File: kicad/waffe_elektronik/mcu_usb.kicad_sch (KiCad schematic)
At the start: 11 parts, among them J3 USB-C (Flashen + Laden), SW3 RESET, SW4 BOOT, U12 USBLC6-2SC6, U4 ESP32-S3-WROOM-1-N16R8

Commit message: Platine: günstigere JLC-Teile, Option ESP32-S3-WROOM-1U mit externer Antenne
- Flash ZD35Q1GC-IB, Kondensatoren/Dioden/Widerstände auf Basic-Teile und 0402, Layout angepasst
- WROOM-1U auf demselben Footprint: eigene JLCPCB-BOM/CPL (Modulmitte 3,15 mm versetzt),
  Mouser-Option mit Pigtail RP-SMA/U.FL und Knick-Stabantenne, 3D-Modell des 1U
- Gerber, BOM, CPL, Renders und Bestelllisten neu erzeugt

Co-Authored-By: Claude Opus 5.5 <noreply@anthropic.com>
Claude-Session: https://claude.ai/code/session_01KkZzubjLKyW9odUwvmxTog
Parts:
- SW3, SW4: LCSC C231329 -> (none)
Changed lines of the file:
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@@
     (instances
       (project "waffe_elektronik"
-        (path "/117486d7-9cbb-4cb5-8faf-1b6e58d9c176"
+        (path "/1905d055-ea1f-4733-9037-b305b5c29de9"
           (reference "U4") (unit 1)
         )
@@
     (instances
       (project "waffe_elektronik"
-        (path "/117486d7-9cbb-4cb5-8faf-1b6e58d9c176"
+        (path "/1905d055-ea1f-4733-9037-b305b5c29de9"
           (reference "#PWR27") (unit 1)
         )
@@
     (instances
       (project "waffe_elektronik"
-        (path "/117486d7-9cbb-4cb5-8faf-1b6e58d9c176"
+        (path "/1905d055-ea1f-4733-9037-b305b5c29de9"
           (reference "C17") (unit 1)
         )
@@
     (instances
       (project "waffe_elektronik"
-        (path "/117486d7-9cbb-4cb5-8faf-1b6e58d9c176"
+        (path "/1905d055-ea1f-4733-9037-b305b5c29de9"
           (reference "#PWR28") (unit 1)
         )
@@
     (instances
       (project "waffe_elektronik"
-        (path "/117486d7-9cbb-4cb5-8faf-1b6e58d9c176"
+        (path "/1905d055-ea1f-4733-9037-b305b5c29de9"
           (reference "C18") (unit 1)
         )
@@
     (instances
       (project "waffe_elektronik"
-        (path "/117486d7-9cbb-4cb5-8faf-1b6e58d9c176"
+        (path "/1905d055-ea1f-4733-9037-b305b5c29de9"
           (reference "#PWR29") (unit 1)
         )
@@
     (instances
       (project "waffe_elektronik"
-        (path "/117486d7-9cbb-4cb5-8faf-1b6e58d9c176"
+        (path "/1905d055-ea1f-4733-9037-b305b5c29de9"
           (reference "#PWR30") (unit 1)
         )
@@
     (instances
       (project "waffe_elektronik"
-        (path "/117486d7-9cbb-4cb5-8faf-1b6e58d9c176"
+        (path "/1905d055-ea1f-4733-9037-b305b5c29de9"
           (reference "R21") (unit 1)
         )
@@
     (instances
       (project "waffe_elektronik"
-        (path "/117486d7-9cbb-4cb5-8faf-1b6e58d9c176"
+        (path "/1905d055-ea1f-4733-9037-b305b5c29de9"
           (reference "#PWR31") (unit 1)
         )
@@
     (instances
       (project "waffe_elektronik"
-        (path "/117486d7-9cbb-4cb5-8faf-1b6e58d9c176"
+        (path "/1905d055-ea1f-4733-9037-b305b5c29de9"
           (reference "C16") (unit 1)
         )
@@
     (instances
       (project "waffe_elektronik"
-        (path "/117486d7-9cbb-4cb5-8faf-1b6e58d9c176"
+        (path "/1905d055-ea1f-4733-9037-b305b5c29de9"
           (reference "#PWR32") (unit 1)
         )
@@
       (effects (font (size 1.27 1.27)) hide)
     )
-    (property "LCSC" "C231329" (at 0 0 0)
-      (effects (font (size 1.27 1.27)) hide)
-    )
-    (pin "1")
-    (pin "2")
-    (instances
-      (project "waffe_elektronik"
-        (path "/117486d7-9cbb-4cb5-8faf-1b6e58d9c176"
+    (pin "1")
+    (pin "2")
+    (instances
+      (project "waffe_elektronik"
+        (path "/1905d055-ea1f-4733-9037-b305b5c29de9"
           (reference "SW3") (unit 1)
         )
@@
     (instances
       (project "waffe_elektronik"
-        (path "/117486d7-9cbb-4cb5-8faf-1b6e58d9c176"
+        (path "/1905d055-ea1f-4733-9037-b305b5c29de9"
           (reference "#PWR33") (unit 1)
         )
@@
       (effects (font (size 1.27 1.27)) hide)
     )
-    (property "LCSC" "C231329" (at 0 0 0)
-      (effects (font (size 1.27 1.27)) hide)
-    )
-    (pin "1")
-    (pin "2")
-    (instances
-      (project "waffe_elektronik"
-        (path "/117486d7-9cbb-4cb5-8faf-1b6e58d9c176"
+    (pin "1")
+    (pin "2")
+    (instances
+      (project "waffe_elektronik"
+        (path "/1905d055-ea1f-4733-9037-b305b5c29de9"
           (reference "SW4") (unit 1)
         )
@@
     (instances
       (project "waffe_elektronik"
-        (path "/117486d7-9cbb-4cb5-8faf-1b6e58d9c176"
+        (path "/1905d055-ea1f-4733-9037-b305b5c29de9"
           (reference "#PWR34") (unit 1)
         )
@@
     (instances
       (project "waffe_elektronik"
-        (path "/117486d7-9cbb-4cb5-8faf-1b6e58d9c176"
+        (path "/1905d055-ea1f-4733-9037-b305b5c29de9"
           (reference "J3") (unit 1)
         )
@@
     (instances
       (project "waffe_elektronik"
-        (path "/117486d7-9cbb-4cb5-8faf-1b6e58d9c176"
+        (path "/1905d055-ea1f-4733-9037-b305b5c29de9"
           (reference "#PWR35") (unit 1)
         )
@@
     (instances
       (project "waffe_elektronik"
-        (path "/117486d7-9cbb-4cb5-8faf-1b6e58d9c176"
+        (path "/1905d055-ea1f-4733-9037-b305b5c29de9"
           (reference "R23") (unit 1)
         )
@@
     (instances
       (project "waffe_elektronik"
-        (path "/117486d7-9cbb-4cb5-8faf-1b6e58d9c176"
+        (path "/1905d055-ea1f-4733-9037-b305b5c29de9"
           (reference "#PWR36") (unit 1)
         )
@@
     (instances
       (project "waffe_elektronik"
-        (path "/117486d7-9cbb-4cb5-8faf-1b6e58d9c176"
+        (path "/1905d055-ea1f-4733-9037-b305b5c29de9"
           (reference "R22") (unit 1)
         )
@@
     (instances
       (project "waffe_elektronik"
-        (path "/117486d7-9cbb-4cb5-8faf-1b6e58d9c176"
+        (path "/1905d055-ea1f-4733-9037-b305b5c29de9"
           (reference "#PWR37") (unit 1)
         )
@@
     (instances
       (project "waffe_elektronik"
-        (path "/117486d7-9cbb-4cb5-8faf-1b6e58d9c176"
+        (path "/1905d055-ea1f-4733-9037-b305b5c29de9"
           (reference "U12") (unit 1)
         )
@@
     (instances
       (project "waffe_elektronik"
-        (path "/117486d7-9cbb-4cb5-8faf-1b6e58d9c176"
+        (path "/1905d055-ea1f-4733-9037-b305b5c29de9"
           (reference "#PWR38") (unit 1)
         )
@@
     (instances
       (project "waffe_elektronik"
-        (path "/117486d7-9cbb-4cb5-8faf-1b6e58d9c176"
+        (path "/1905d055-ea1f-4733-9037-b305b5c29de9"
           (reference "#PWR39") (unit 1)
         )
@@
     (instances
       (project "waffe_elektronik"
-        (path "/117486d7-9cbb-4cb5-8faf-1b6e58d9c176"
+        (path "/1905d055-ea1f-4733-9037-b305b5c29de9"
           (reference "#PWR40") (unit 1)
         )

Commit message: Fertigung: JLCPCB-BOM/CPL mit allen Steckern und Tastern (Variante komplett)
- Handlötteile tragen im Schaltplan das Feld "LCSC Hand" statt "LCSC", build_board.py übernimmt es
- jlc_fab.py schreibt zusätzlich *_komplett und *_komplett_externe_antenne (79 Teile, 20 Extended),
  --check prüft den Bedarf der Komplett-Variante; Rotationskorrektur 180° für JST-SH (ungeprüft)
- Schaltplan und Platine neu erzeugt (Geometrie unverändert), Gerber neu, Doku angepasst

Co-Authored-By: Claude Opus 5.5 <noreply@anthropic.com>
Claude-Session: https://claude.ai/code/session_01KkZzubjLKyW9odUwvmxTog
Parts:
- SW3, SW4: LCSC Hand (none) -> C231329
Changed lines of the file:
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@@
     (instances
       (project "waffe_elektronik"
-        (path "/1905d055-ea1f-4733-9037-b305b5c29de9"
+        (path "/3bcff933-1787-416b-898f-1e2cea15666c"
           (reference "U4") (unit 1)
         )
@@
     (instances
       (project "waffe_elektronik"
-        (path "/1905d055-ea1f-4733-9037-b305b5c29de9"
+        (path "/3bcff933-1787-416b-898f-1e2cea15666c"
           (reference "#PWR27") (unit 1)
         )
@@
     (instances
       (project "waffe_elektronik"
-        (path "/1905d055-ea1f-4733-9037-b305b5c29de9"
+        (path "/3bcff933-1787-416b-898f-1e2cea15666c"
           (reference "C17") (unit 1)
         )
@@
     (instances
       (project "waffe_elektronik"
-        (path "/1905d055-ea1f-4733-9037-b305b5c29de9"
+        (path "/3bcff933-1787-416b-898f-1e2cea15666c"
           (reference "#PWR28") (unit 1)
         )
@@
     (instances
       (project "waffe_elektronik"
-        (path "/1905d055-ea1f-4733-9037-b305b5c29de9"
+        (path "/3bcff933-1787-416b-898f-1e2cea15666c"
           (reference "C18") (unit 1)
         )
@@
     (instances
       (project "waffe_elektronik"
-        (path "/1905d055-ea1f-4733-9037-b305b5c29de9"
+        (path "/3bcff933-1787-416b-898f-1e2cea15666c"
           (reference "#PWR29") (unit 1)
         )
@@
     (instances
       (project "waffe_elektronik"
-        (path "/1905d055-ea1f-4733-9037-b305b5c29de9"
+        (path "/3bcff933-1787-416b-898f-1e2cea15666c"
           (reference "#PWR30") (unit 1)
         )
@@
     (instances
       (project "waffe_elektronik"
-        (path "/1905d055-ea1f-4733-9037-b305b5c29de9"
+        (path "/3bcff933-1787-416b-898f-1e2cea15666c"
           (reference "R21") (unit 1)
         )
@@
     (instances
       (project "waffe_elektronik"
-        (path "/1905d055-ea1f-4733-9037-b305b5c29de9"
+        (path "/3bcff933-1787-416b-898f-1e2cea15666c"
           (reference "#PWR31") (unit 1)
         )
@@
     (instances
       (project "waffe_elektronik"
-        (path "/1905d055-ea1f-4733-9037-b305b5c29de9"
+        (path "/3bcff933-1787-416b-898f-1e2cea15666c"
           (reference "C16") (unit 1)
         )
@@
     (instances
       (project "waffe_elektronik"
-        (path "/1905d055-ea1f-4733-9037-b305b5c29de9"
+        (path "/3bcff933-1787-416b-898f-1e2cea15666c"
           (reference "#PWR32") (unit 1)
         )
@@
       (effects (font (size 1.27 1.27)) hide)
     )
-    (pin "1")
-    (pin "2")
-    (instances
-      (project "waffe_elektronik"
-        (path "/1905d055-ea1f-4733-9037-b305b5c29de9"
+    (property "LCSC Hand" "C231329" (at 0 0 0)
+      (effects (font (size 1.27 1.27)) hide)
+    )
+    (pin "1")
+    (pin "2")
+    (instances
+      (project "waffe_elektronik"
+        (path "/3bcff933-1787-416b-898f-1e2cea15666c"
           (reference "SW3") (unit 1)
         )
@@
     (instances
       (project "waffe_elektronik"
-        (path "/1905d055-ea1f-4733-9037-b305b5c29de9"
+        (path "/3bcff933-1787-416b-898f-1e2cea15666c"
           (reference "#PWR33") (unit 1)
         )
@@
       (effects (font (size 1.27 1.27)) hide)
     )
-    (pin "1")
-    (pin "2")
-    (instances
-      (project "waffe_elektronik"
-        (path "/1905d055-ea1f-4733-9037-b305b5c29de9"
+    (property "LCSC Hand" "C231329" (at 0 0 0)
+      (effects (font (size 1.27 1.27)) hide)
+    )
+    (pin "1")
+    (pin "2")
+    (instances
+      (project "waffe_elektronik"
+        (path "/3bcff933-1787-416b-898f-1e2cea15666c"
           (reference "SW4") (unit 1)
         )
@@
     (instances
       (project "waffe_elektronik"
-        (path "/1905d055-ea1f-4733-9037-b305b5c29de9"
+        (path "/3bcff933-1787-416b-898f-1e2cea15666c"
           (reference "#PWR34") (unit 1)
         )
@@
     (instances
       (project "waffe_elektronik"
-        (path "/1905d055-ea1f-4733-9037-b305b5c29de9"
+        (path "/3bcff933-1787-416b-898f-1e2cea15666c"
           (reference "J3") (unit 1)
         )
@@
     (instances
       (project "waffe_elektronik"
-        (path "/1905d055-ea1f-4733-9037-b305b5c29de9"
+        (path "/3bcff933-1787-416b-898f-1e2cea15666c"
           (reference "#PWR35") (unit 1)
         )
@@
     (instances
       (project "waffe_elektronik"
-        (path "/1905d055-ea1f-4733-9037-b305b5c29de9"
+        (path "/3bcff933-1787-416b-898f-1e2cea15666c"
           (reference "R23") (unit 1)
         )
@@
     (instances
       (project "waffe_elektronik"
-        (path "/1905d055-ea1f-4733-9037-b305b5c29de9"
+        (path "/3bcff933-1787-416b-898f-1e2cea15666c"
           (reference "#PWR36") (unit 1)
         )
@@
     (instances
       (project "waffe_elektronik"
-        (path "/1905d055-ea1f-4733-9037-b305b5c29de9"
+        (path "/3bcff933-1787-416b-898f-1e2cea15666c"
           (reference "R22") (unit 1)
         )
@@
     (instances
       (project "waffe_elektronik"
-        (path "/1905d055-ea1f-4733-9037-b305b5c29de9"
+        (path "/3bcff933-1787-416b-898f-1e2cea15666c"
           (reference "#PWR37") (unit 1)
         )
@@
     (instances
       (project "waffe_elektronik"
-        (path "/1905d055-ea1f-4733-9037-b305b5c29de9"
+        (path "/3bcff933-1787-416b-898f-1e2cea15666c"
           (reference "U12") (unit 1)
         )
@@
     (instances
       (project "waffe_elektronik"
-        (path "/1905d055-ea1f-4733-9037-b305b5c29de9"
+        (path "/3bcff933-1787-416b-898f-1e2cea15666c"
           (reference "#PWR38") (unit 1)
         )
@@
     (instances
       (project "waffe_elektronik"
-        (path "/1905d055-ea1f-4733-9037-b305b5c29de9"
+        (path "/3bcff933-1787-416b-898f-1e2cea15666c"
           (reference "#PWR39") (unit 1)
         )
@@
     (instances
       (project "waffe_elektronik"
-        (path "/1905d055-ea1f-4733-9037-b305b5c29de9"
+        (path "/3bcff933-1787-416b-898f-1e2cea15666c"
           (reference "#PWR40") (unit 1)
         )

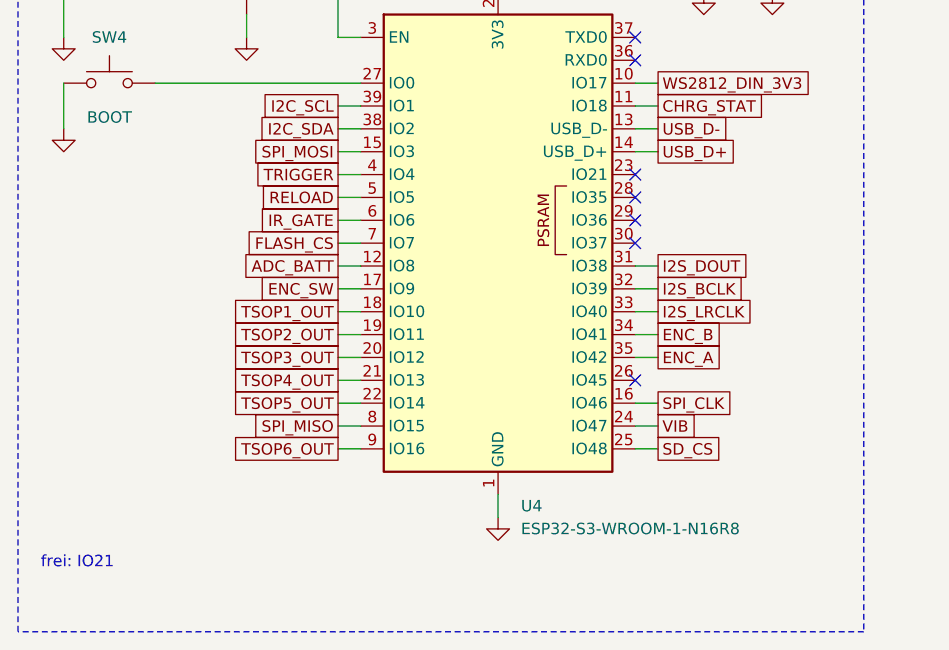
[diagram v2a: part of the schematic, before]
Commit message: Platine: microSD-Slot gedreht, Ein/Aus über den Drehgeber-Taster, R7 12 Ω, 10 µF am Slot
- J7: Karte wird auf der Kontaktseite eingesteckt (Datenblatt TF-018) -> Slot gedreht, Kontakte und
  Öffnung an der Unterkante, SD-Leitungen neu verlegt
- Soft-Power: Q4 (AO3401A) trennt den Akku von BAT_SW, Taster an J5.2 schaltet über D6 (BAT54CW) ein,
  IO21 hält über Q5, IO9 liest den Taster; Lasche oben links 18,6 x 9 mm mit den neuen Teilen,
  Leitungen auf B.Cu über die Oberkante, Akku-Plus über In2
- R7 12 Ω (C17913), C28 10 µF an der microSD-Versorgung
- Gerber, BOM/CPL (alle Varianten), Mouser-BOM, Renders und Doku neu

Co-Authored-By: Claude Opus 5.5 <noreply@anthropic.com>
Claude-Session: https://claude.ai/code/session_01KkZzubjLKyW9odUwvmxTog
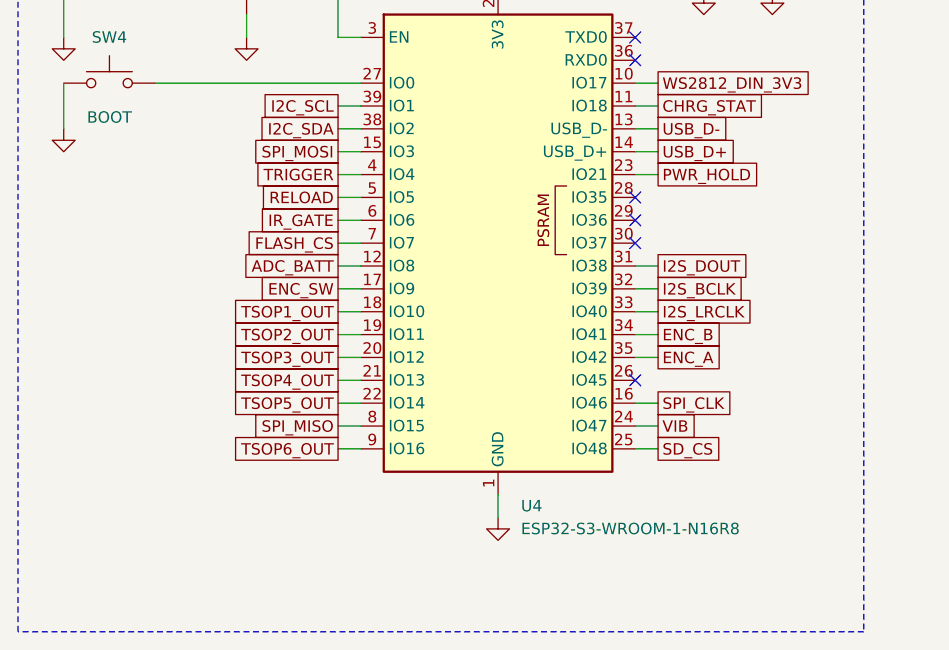
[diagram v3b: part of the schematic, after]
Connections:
- net PWR_HOLD: now reaches U4.23 (IO21)
- no-connect marks 9 -> 8
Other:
- note removed: "frei: IO21"

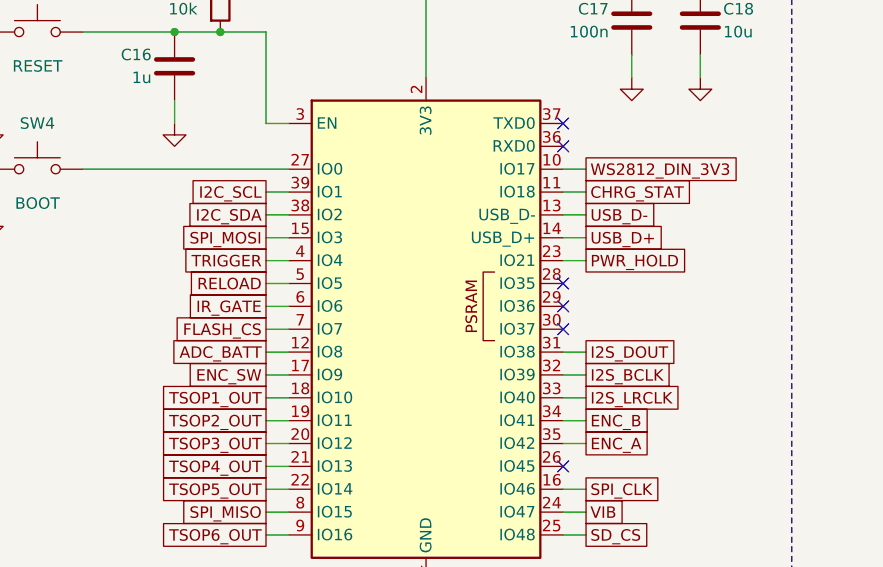
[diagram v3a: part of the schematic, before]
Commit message: Platine: IP5306 (2 A Laden + 5 V) statt MT3608/MCP73831, Ein/Aus über KEY, eigener I²C-Bus
Co-Authored-By: Claude Opus 5.5 <noreply@anthropic.com>
Claude-Session: https://claude.ai/code/session_01KkZzubjLKyW9odUwvmxTog
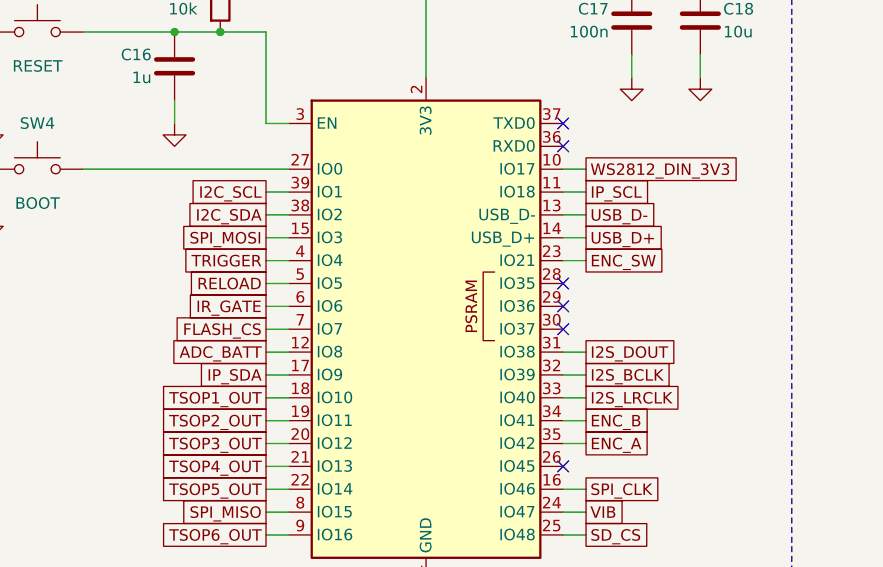
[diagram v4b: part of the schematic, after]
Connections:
- net PWR_HOLD is gone; now on net ENC_SW: U4.23 (IO21)
- net ENC_SW: no longer U4.17 (IO9)
- net CHRG_STAT renamed IP_SCL
- new net IP_SDA: U4.17 (IO9)
